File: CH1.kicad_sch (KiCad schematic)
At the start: 28 parts, among them IC201 TS12A4516DBVR, J101 CH1, SW101 /10, SW101 AC/DC, U102 OPA356xxDBV, U104 OPA356xxDBV, U203 TLP176AM

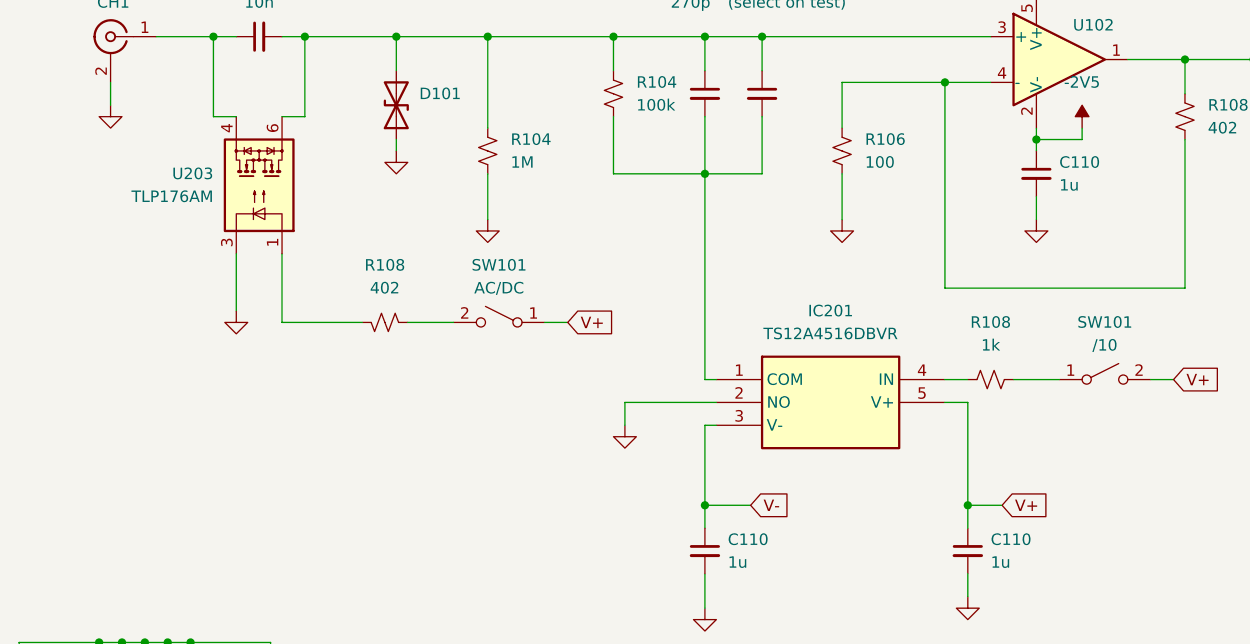
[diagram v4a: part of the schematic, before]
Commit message: mux in mistake fix
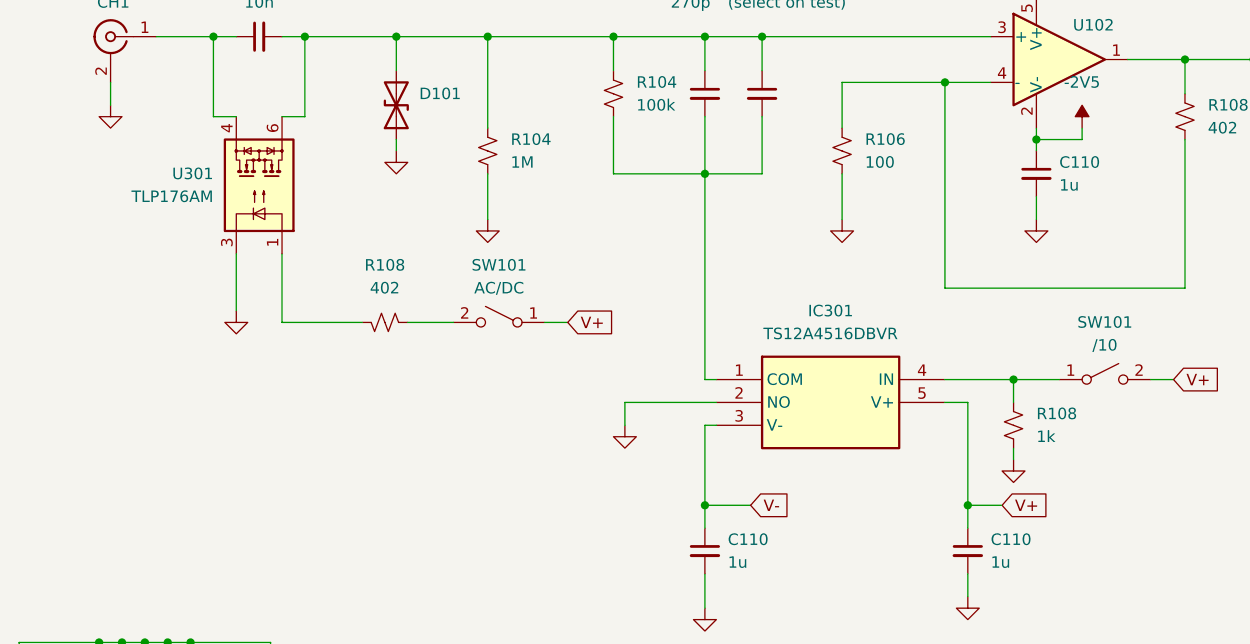
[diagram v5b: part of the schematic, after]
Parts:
- renumbered IC201 to IC301, U203 to U301
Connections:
- net GND: now also R108.2
- net at IC301.4 (IN): now also R108.1, SW101.1 (A); no longer R108.2
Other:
- moved on the sheet: R108
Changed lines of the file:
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@@
   (junction (at 43.18 148.59) (diameter 0) (color 0 0 0 0)
   )
+  (junction (at 153.67 100.33) (diameter 0) (color 0 0 0 0)
+  )
   (junction (at 71.12 146.05) (diameter 0) (color 0 0 0 0)
   )
@@
     (stroke (width 0) (type default))
   )
-  (wire (pts (xy 158.75 100.33) (xy 153.67 100.33))
-    (stroke (width 0) (type default))
-  )
   (wire (pts (xy 156.21 73.66) (xy 156.21 74.93))
     (stroke (width 0) (type default))
@@
     (stroke (width 0) (type default))
   )
+  (wire (pts (xy 153.67 102.87) (xy 153.67 100.33))
+    (stroke (width 0) (type default))
+  )
   (wire (pts (xy 72.39 71.12) (xy 74.93 71.12))
     (stroke (width 0) (type default))
@@
     (stroke (width 0) (type default))
   )
+  (wire (pts (xy 146.05 100.33) (xy 153.67 100.33))
+    (stroke (width 0) (type default))
+  )
   (wire (pts (xy 43.18 146.05) (xy 43.18 143.51))
     (stroke (width 0) (type default))
@@
     (stroke (width 0) (type default))
   )
-  (wire (pts (xy 148.59 100.33) (xy 146.05 100.33))
-    (stroke (width 0) (type default))
-  )
   (wire (pts (xy 199.39 67.31) (xy 205.74 67.31))
     (stroke (width 0) (type default))
@@
     (stroke (width 0) (type default))
   )
+  (wire (pts (xy 153.67 107.95) (xy 153.67 109.22))
+    (stroke (width 0) (type default))
+  )
   (wire (pts (xy 171.45 100.33) (xy 168.91 100.33))
     (stroke (width 0) (type default))
@@
   )
   (wire (pts (xy 85.09 73.66) (xy 85.09 74.93))
+    (stroke (width 0) (type default))
+  )
+  (wire (pts (xy 153.67 100.33) (xy 158.75 100.33))
     (stroke (width 0) (type default))
   )
@@
   (symbol (lib_id "Relay_SolidState:TLP175A") (at 69.85 78.74 270) (mirror x) (unit 1)
     (in_bom yes) (on_board yes) (dnp no)
-    (property "Reference" "U203" (at 64.77 77.47 90)
+    (property "Reference" "U301" (at 64.77 77.47 90)
       (effects (font (size 1.27 1.27)) (justify right))
     )
@@
   (symbol (lib_id "TS12A4516:TS12A4516DBVR") (at 120.65 100.33 0) (unit 1)
     (in_bom yes) (on_board yes) (dnp no) (fields_autoplaced)
-    (property "Reference" "IC201" (at 133.35 92.71 0)
+    (property "Reference" "IC301" (at 133.35 92.71 0)
       (effects (font (size 1.27 1.27)))
     )
@@
     )
   )
+  (symbol (lib_id "power:GND") (at 153.67 109.22 0) (unit 1)
+    (in_bom yes) (on_board yes) (dnp no) (fields_autoplaced)
+    (property "Reference" "#PWR0114" (at 153.67 115.57 0)
+      (effects (font (size 1.27 1.27)) hide)
+    )
+    (property "Value" "GND" (at 153.67 114.3 0)
+      (effects (font (size 1.27 1.27)) hide)
+    )
+    (property "Footprint" "" (at 153.67 109.22 0)
+      (effects (font (size 1.27 1.27)) hide)
+    )
+    (property "Datasheet" "" (at 153.67 109.22 0)
+      (effects (font (size 1.27 1.27)) hide)
+    )
+    (pin "1")
+    (instances
+      (project "AD3 Front End Amplifier"
+        (path "/9ac7c606-b6c4-44a9-a37a-81b4304cf499"
+          (reference "#PWR0114") (unit 1)
+        )
+        (path "/9ac7c606-b6c4-44a9-a37a-81b4304cf499/945c961b-dd89-4094-9375-4427d09c7e83"
+          (reference "#PWR0319") (unit 1)
+        )
+        (path "/9ac7c606-b6c4-44a9-a37a-81b4304cf499/201ab37e-dba2-4bc7-be1e-9a5dcf71f665"
+          (reference "#PWR0219") (unit 1)
+        )
+      )
+    )
+  )
   (symbol (lib_id "Device:C_Small") (at 199.39 95.25 0) (unit 1)
     (in_bom yes) (on_board yes) (dnp no)
@@
     )
   )
-  (symbol (lib_id "Device:R_Small_US") (at 151.13 100.33 270) (unit 1)
-    (in_bom yes) (on_board yes) (dnp no) (fields_autoplaced)
-    (property "Reference" "R108" (at 151.13 93.98 90)
-      (effects (font (size 1.27 1.27)))
-    )
-    (property "Value" "1k" (at 151.13 96.52 90)
-      (effects (font (size 1.27 1.27)))
-    )
-    (property "Footprint" "Resistor_SMD:R_0402_1005Metric_Pad0.72x0.64mm_HandSolder" (at 151.13 100.33 0)
-      (effects (font (size 1.27 1.27)) hide)
-    )
-    (property "Datasheet" "~" (at 151.13 100.33 0)
-      (effects (font (size 1.27 1.27)) hide)
-    )
-    (property "Part Number" "" (at 151.13 100.33 0)
-      (effects (font (size 1.27 1.27)) hide)
-    )
+  (symbol (lib_id "Device:R_Small_US") (at 153.67 105.41 0) (unit 1)
+    (in_bom yes) (on_board yes) (dnp no) (fields_autoplaced)
+    (property "Reference" "R108" (at 156.21 104.14 0)
+      (effects (font (size 1.27 1.27)) (justify left))
+    )
+    (property "Value" "1k" (at 156.21 106.68 0)
+      (effects (font (size 1.27 1.27)) (justify left))
+    )
+    (property "Footprint" "Resistor_SMD:R_0402_1005Metric_Pad0.72x0.64mm_HandSolder" (at 153.67 105.41 0)
+      (effects (font (size 1.27 1.27)) hide)
+    )
+    (property "Datasheet" "~" (at 153.67 105.41 0)
+      (effects (font (size 1.27 1.27)) hide)
+    )
+    (property "Part Number" "" (at 153.67 105.41 0)
+      (effects (font (size 1.27 1.27)) hide)
+    )

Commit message: MK3
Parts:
- C101: value 270p -> 1n
- C103: value 10n -> 100n; Part Number ECH-U1C103JX5 -> (none)
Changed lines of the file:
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@@
       (effects (font (size 1.27 1.27)) (justify left))
     )
-    (property "Value" "270p" (at 115.57 58.42 0)
+    (property "Value" "1n" (at 115.57 58.42 0)
       (effects (font (size 1.27 1.27)) (justify left))
     )
@@
       (effects (font (size 1.27 1.27)))
     )
-    (property "Value" "10n" (at 69.8563 58.42 90)
+    (property "Value" "100n" (at 69.8563 58.42 90)
       (effects (font (size 1.27 1.27)))
     )
@@
       (effects (font (size 1.27 1.27)) hide)
     )
-    (property "Part Number" "ECH-U1C103JX5" (at 69.85 62.23 0)
-      (effects (font (size 1.27 1.27)) hide)
-    )
+    (property "Part Number" "" (at 69.85 62.23 0)
+      (effects (font (size 1.27 1.27)) hide)
+    )
